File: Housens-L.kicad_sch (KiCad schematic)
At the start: 44 parts, among them J1 JTAG/SWD, J2 USB_C_2.0, Q1 DMC3071LVT, SW1 RESET, SW2 USER_BTN, U1 MCP1603, U2 BME280, U3 OPT3005, U4 STM32WB55CGUx, Y1 32MHz, Y2 32.768kHz

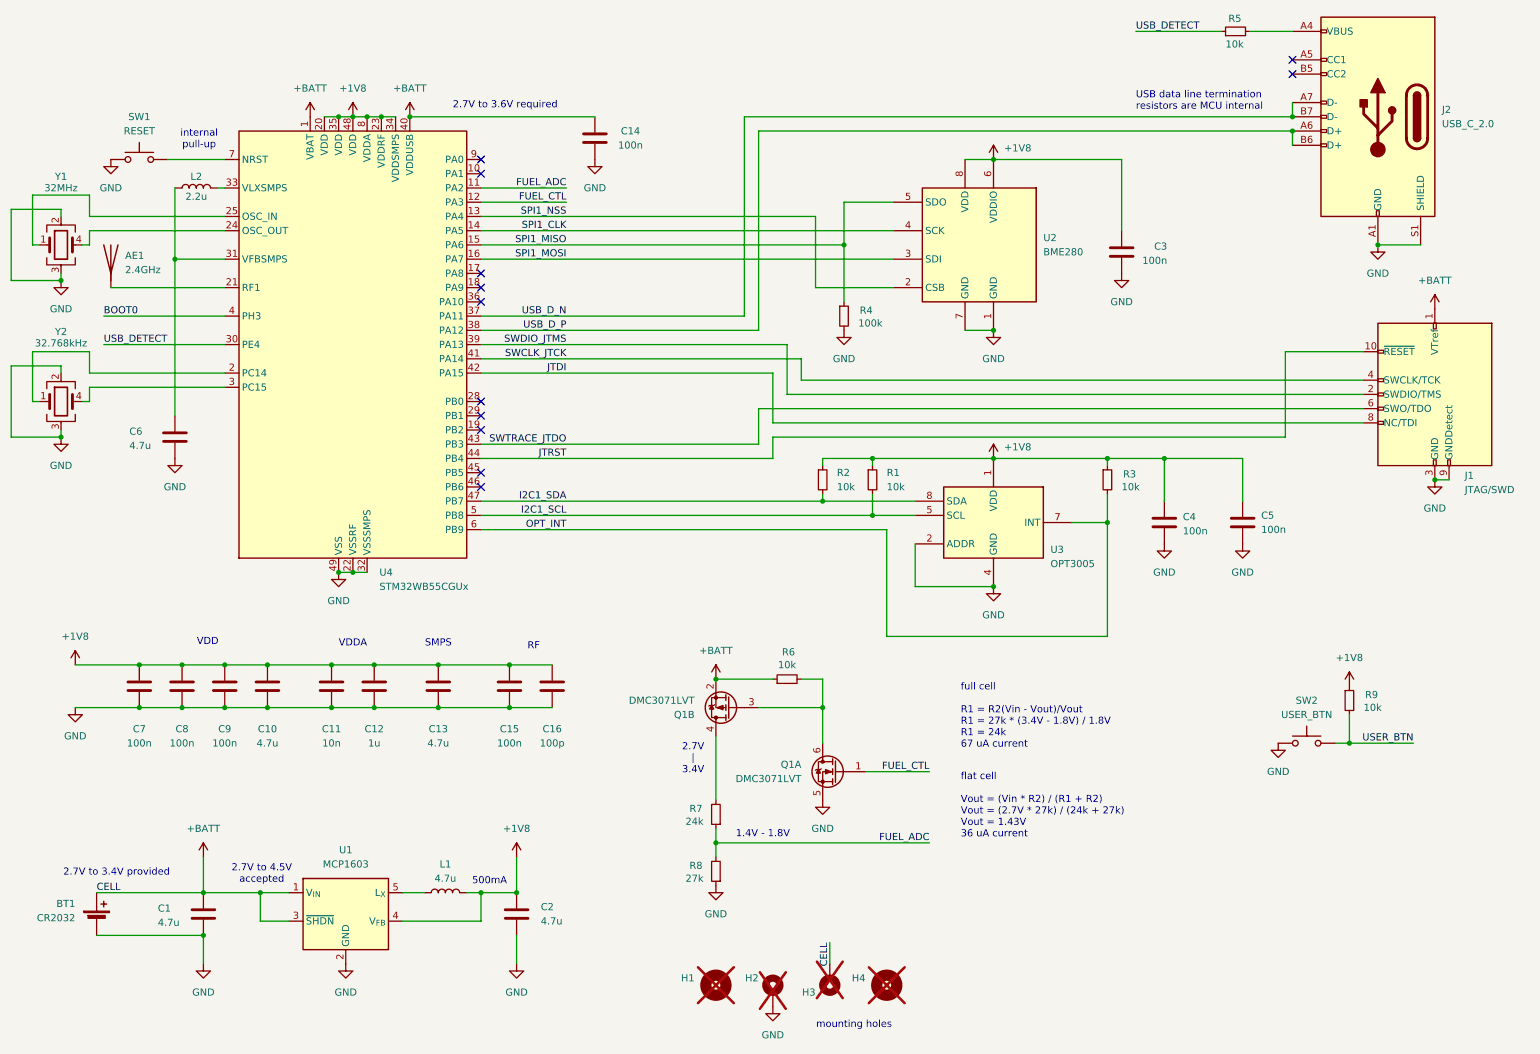
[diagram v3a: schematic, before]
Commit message: Layout 1V8 and USB
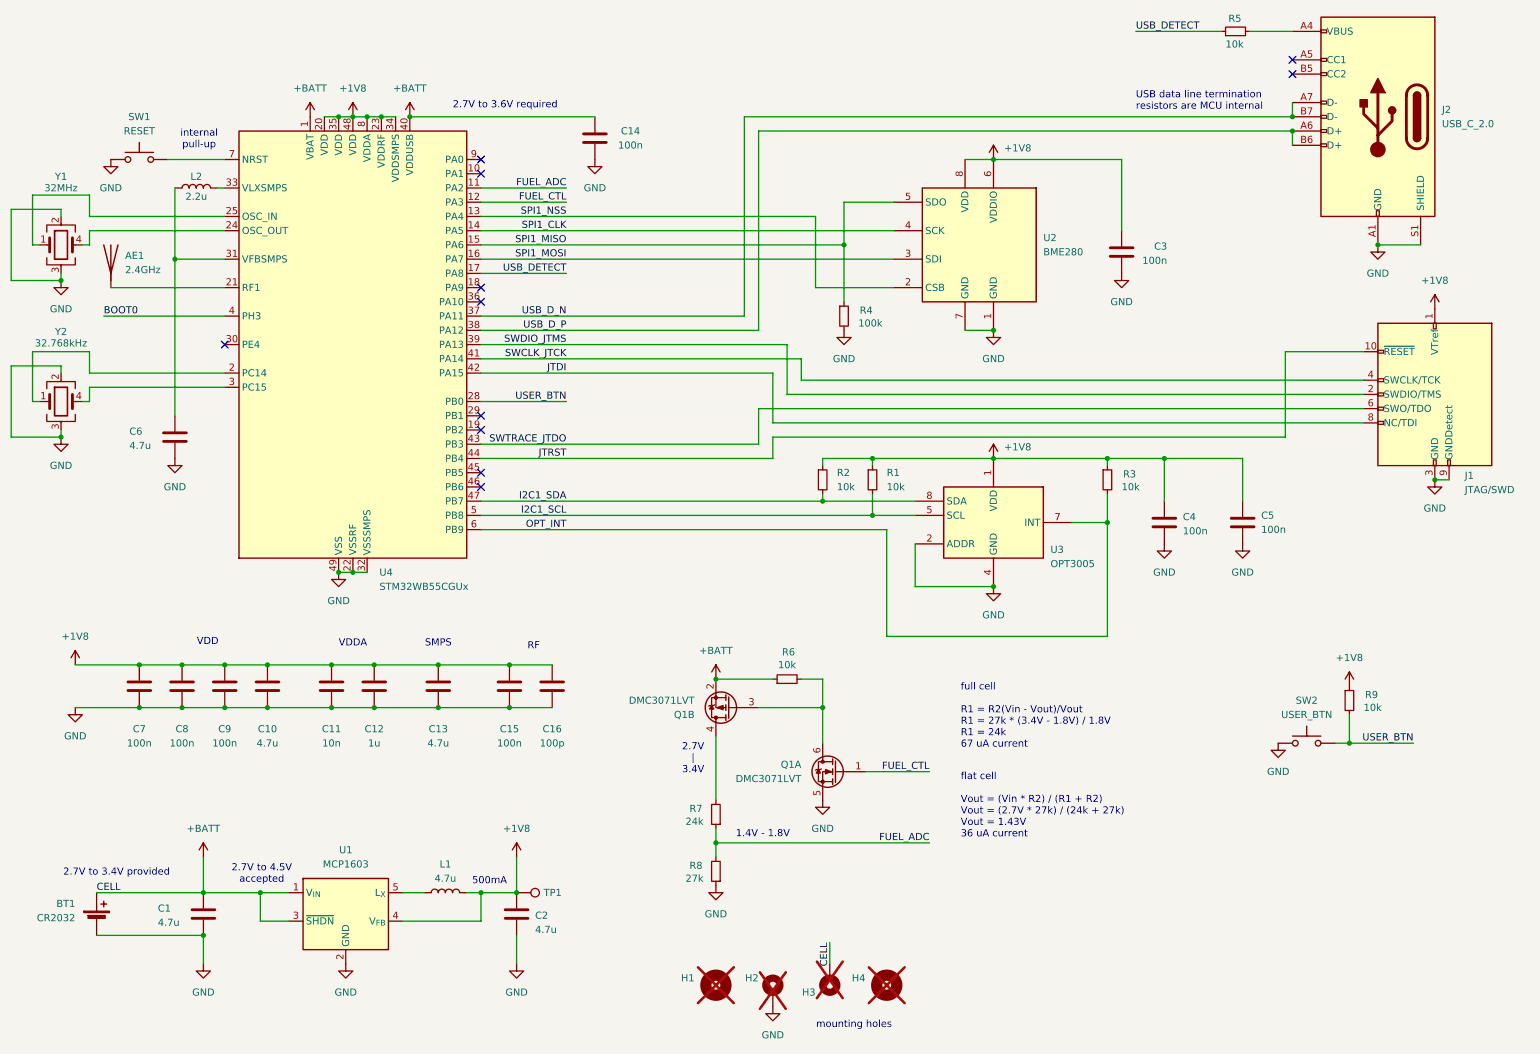
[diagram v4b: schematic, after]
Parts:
- added TP1: TestPoint, TestPoint:TestPoint_Pad_D2.0mm, symbol Connector:TestPoint
- J2: footprint Connector_USB:USB_C_Receptacle_G-Switch_GT-USB-7010ASV -> Connector_USB:USB_C_Receptacle_GCT_USB4085
- L1, L2: footprint Inductor_SMD:L_Wuerth_WE-TPC-3816 -> Imported:L_Wuerth_WE-TPC-2811
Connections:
- net +1V8: now also J1.1 (VTref), TP1.1
- net +BATT: no longer J1.1 (VTref)
- net USB_DETECT: now also U4.17 (PA8); no longer U4.30 (PE4)
- net USER_BTN: now also U4.28 (PB0)
- no-connect marks 12 -> 11
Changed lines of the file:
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@@
 	)
 	(no_connect
-		(at 99.06 82.55)
-	)
-	(no_connect
 		(at 99.06 87.63)
 	)
@@
 	)
 	(no_connect
-		(at 99.06 59.69)
-	)
-	(no_connect
 		(at 99.06 64.77)
 	)
@@
 	)
 	(no_connect
+		(at 53.34 72.39)
+	)
+	(no_connect
 		(at 99.06 62.23)
 	)
@@
 	(wire
 		(pts
-			(xy 160.02 92.71) (xy 168.91 92.71)
+			(xy 99.06 82.55) (xy 114.3 82.55)
 		)
 		(stroke
@@
 	(wire
 		(pts
-			(xy 76.2 31.75) (xy 78.74 31.75)
+			(xy 160.02 92.71) (xy 168.91 92.71)
 		)
 		(stroke
@@
 	(wire
 		(pts
-			(xy 105.41 163.83) (xy 105.41 170.18)
+			(xy 76.2 31.75) (xy 78.74 31.75)
 		)
 		(stroke
@@
 	(wire
 		(pts
-			(xy 73.66 31.75) (xy 76.2 31.75)
+			(xy 105.41 163.83) (xy 105.41 170.18)
 		)
 		(stroke
@@
 	(wire
 		(pts
-			(xy 24.13 76.2) (xy 15.24 76.2)
+			(xy 73.66 31.75) (xy 76.2 31.75)
 		)
 		(stroke
@@
 	(wire
 		(pts
-			(xy 140.97 142.24) (xy 140.97 153.67)
+			(xy 24.13 76.2) (xy 15.24 76.2)
 		)
 		(stroke
@@
 	(wire
 		(pts
-			(xy 31.75 72.39) (xy 53.34 72.39)
+			(xy 140.97 142.24) (xy 140.97 153.67)
 		)
 		(stroke
@@
 	(wire
 		(pts
+			(xy 99.06 59.69) (xy 114.3 59.69)
+		)
+		(stroke
+			(width 0)
+			(type default)
+		)
+	)
+	(wire
+		(pts
 			(xy 80.01 129.54) (xy 91.44 129.54)
 		)
@@
 		)
 	)
+	(label "USER_BTN"
+		(at 114.3 82.55 180)
+		(fields_autoplaced yes)
+		(effects
+			(font
+				(size 1.27 1.27)
+			)
+			(justify right bottom)
+		)
+	)
 	(label "FUEL_ADC"
 		(at 114.3 44.45 180)
@@
 	)
 	(label "USB_DETECT"
-		(at 31.75 72.39 0)
+		(at 114.3 59.69 180)
 		(fields_autoplaced yes)
 		(effects
@@
 				(size 1.27 1.27)
 			)
-			(justify left bottom)
+			(justify right bottom)
 		)
 	)
@@
 			)
 		)
-		(property "Footprint" "Connector_USB:USB_C_Receptacle_G-Switch_GT-USB-7010ASV"
+		(property "Footprint" "Connector_USB:USB_C_Receptacle_GCT_USB4085"
 			(at 255.27 31.75 0)
 			(effects
@@
 	)
 	(symbol
-		(lib_id "power:+BATT")
-		(at 269.24 66.04 0)
-		(unit 1)
-		(exclude_from_sim no)
-		(in_bom yes)
-		(on_board yes)
-		(dnp no)
-		(fields_autoplaced yes)
-		(property "Reference" "#PWR023"
-			(at 269.24 69.85 0)
-			(effects
-				(font
-					(size 1.27 1.27)
-				)
-				(hide yes)
-			)
-		)
-		(property "Value" "+BATT"
-			(at 269.24 60.96 0)
-			(effects
-				(font
-					(size 1.27 1.27)
-				)
-			)
-		)
-		(property "Footprint" ""
-			(at 269.24 66.04 0)
-			(effects
-				(font
-					(size 1.27 1.27)
-				)
-				(hide yes)
-			)
-		)
-		(property "Datasheet" ""
-			(at 269.24 66.04 0)
-			(effects
-				(font
-					(size 1.27 1.27)
-				)
-				(hide yes)
-			)
-		)
-		(property "Description" "Power symbol creates a global label with name \"+BATT\""
-			(at 269.24 66.04 0)
-			(effects
-				(font
-					(size 1.27 1.27)
-				)
-				(hide yes)
-			)
-		)
-		(pin "1"
-		)
-		(instances
-			(project "Housens-L"
-				(path "/36bb4837-104c-4aa4-b300-0e6d0ff24db5"
-					(reference "#PWR023")
-					(unit 1)
-				)
-			)
-		)
-	)
-	(symbol
 		(lib_id "power:GND")
 		(at 73.66 113.03 0)
@@
 			)
 		)
-		(property "Footprint" "Inductor_SMD:L_Wuerth_WE-TPC-3816"
+		(property "Footprint" "Imported:L_Wuerth_WE-TPC-2811"
 			(at 92.71 170.18 0)
 			(effects
@@
 			)
 		)
-		(property "Datasheet" "~"
+		(property "Datasheet" "https://www.we-online.com/components/products/datasheet/744028004.pdf"
 			(at 92.71 170.18 0)
 			(effects
@@
 			)
 		)
-		(property "Description" "Inductor"
+		(property "Description" "WE-TPC SMT Shielded Tiny Power Inductor, 4.7uH"
 			(at 92.71 170.18 0)
 			(effects
@@
 	)
 	(symbol
+		(lib_id "Connector:TestPoint")
+		(at 105.41 170.18 270)
+		(unit 1)
+		(exclude_from_sim no)
+		(in_bom yes)
+		(on_board yes)
+		(dnp no)
+		(property "Reference" "TP1"
+			(at 110.236 170.18 90)
+			(effects
+				(font
+					(size 1.27 1.27)
+				)
+				(justify left)
+			)
+		)
+		(property "Value" "TestPoint"
+			(at 110.49 171.4499 90)
+			(effects
+				(font
+					(size 1.27 1.27)
+				)
+				(justify left)
+				(hide yes)
+			)
+		)
+		(property "Footprint" "TestPoint:TestPoint_Pad_D2.0mm"
+			(at 105.41 175.26 0)
+			(effects
+				(font
+					(size 1.27 1.27)
+				)
+				(hide yes)
+			)
+		)
+		(property "Datasheet" "~"
+			(at 105.41 175.26 0)
+			(effects
+				(font
+					(size 1.27 1.27)
+				)
+				(hide yes)
+			)
+		)
+		(property "Description" "test point"
+			(at 105.41 170.18 0)
+			(effects
+				(font
+					(size 1.27 1.27)
+				)
+				(hide yes)
+			)
+		)
+		(pin "1"
+		)
+		(instances
+			(project ""
+				(path "/36bb4837-104c-4aa4-b300-0e6d0ff24db5"
+					(reference "TP1")
+					(unit 1)
+				)
+			)
+		)
+	)
+	(symbol
 		(lib_id "power:GND")
 		(at 269.24 96.52 0)
@@
 			)
 		)
-		(property "Footprint" "Inductor_SMD:L_Wuerth_WE-TPC-3816"
+		(property "Footprint" "Imported:L_Wuerth_WE-TPC-2811"
 			(at 48.26 44.45 0)
 			(effects
@@
 			)
 		)
-		(property "Datasheet" "~"
+		(property "Datasheet" "https://www.we-online.com/components/products/datasheet/744028002.pdf"
 			(at 48.26 44.45 0)
 			(effects
@@
 			)
 		)
-		(property "Description" "Inductor"
+		(property "Description" "WE-TPC SMT Shielded Tiny Power Inductor, 2.2uH"
 			(at 48.26 44.45 0)
 			(effects
@@
 		(dnp no)
 		(property "Reference" "C2"
-			(at 109.728 172.72 0)
+			(at 108.712 174.244 0)
 			(effects
 				(font
@@
 		)
 		(property "Value" "4.7u"
-			(at 109.728 175.26 0)
+			(at 108.712 176.784 0)
 			(effects
 				(font
@@
 					(unit 1)
 				)
+			)
+		)
+	)
+	(symbol
+		(lib_id "power:+1V8")
+		(at 269.24 66.04 0)
+		(unit 1)
+		(exclude_from_sim no)
+		(in_bom yes)
+		(on_board yes)
+		(dnp no)
+		(fields_autoplaced yes)
+		(property "Reference" "#PWR023"
+			(at 269.24 69.85 0)
+			(effects
+				(font
+					(size 1.27 1.27)
+				)
+				(hide yes)
+			)
+		)
+		(property "Value" "+1V8"
+			(at 269.24 60.96 0)
+			(effects
+				(font
+					(size 1.27 1.27)
+				)
+			)
+		)
+		(property "Footprint" ""
+			(at 269.24 66.04 0)
+			(effects
+				(font
+					(size 1.27 1.27)
+				)
+				(hide yes)
+			)
+		)
+		(property "Datasheet" ""
+			(at 269.24 66.04 0)
+			(effects
+				(font
+					(size 1.27 1.27)
+				)
+				(hide yes)
+			)
+		)
+		(property "Description" "Power symbol creates a global label with name \"+1V8\""
+			(at 269.24 66.04 0)
+			(effects
+				(font
+					(size 1.27 1.27)
+				)
+				(hide yes)
+			)
+		)
+		(pin "1"
+		)
+		(instances
+			(project "Housens-L"
+				(path "/36bb4837-104c-4aa4-b300-0e6d0ff24db5"
+					(reference "#PWR023")
+					(unit 1)
+				)

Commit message: Add 3D model for cell holder
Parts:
- BT1: footprint Battery:BatteryHolder_Keystone_3002_1x2032 -> Invented:BAT-HLD-001_3Pins
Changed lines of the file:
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@@
 			)
 		)
-		(property "Footprint" "Battery:BatteryHolder_Keystone_3002_1x2032"
+		(property "Footprint" "Invented:BAT-HLD-001_3Pins"
 			(at 30.48 173.736 90)
 			(effects
@@
 			)
 		)
-		(property "Datasheet" "~"
+		(property "Datasheet" "https://www.mouser.com/datasheet/2/418/9/LNNC_S_A0002913840_1-3237435.pdf"
 			(at 30.48 173.736 90)
 			(effects
@@
 			)
 		)
-		(property "Description" "Single-cell battery"
+		(property "Description" "Linx/TE SMT Battery Holder for CR2032/CR2025"
 			(at 30.48 175.26 0)
 			(effects

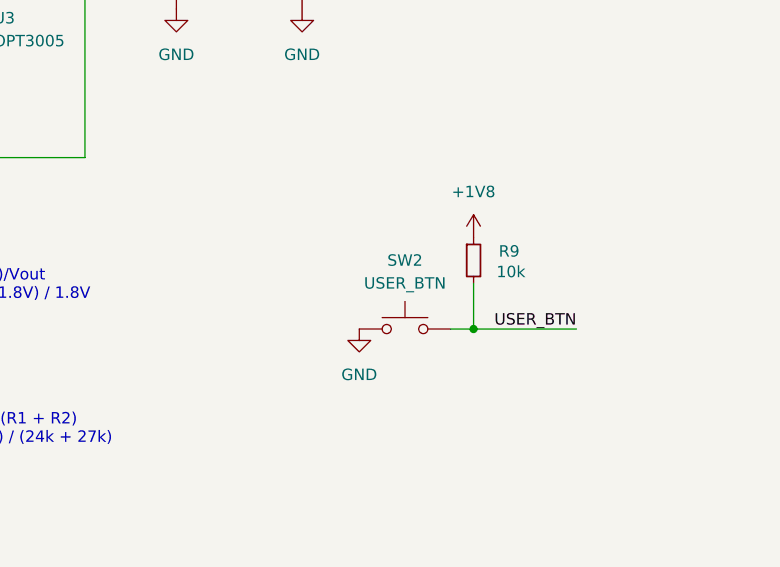
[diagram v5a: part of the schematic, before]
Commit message: Show some labels
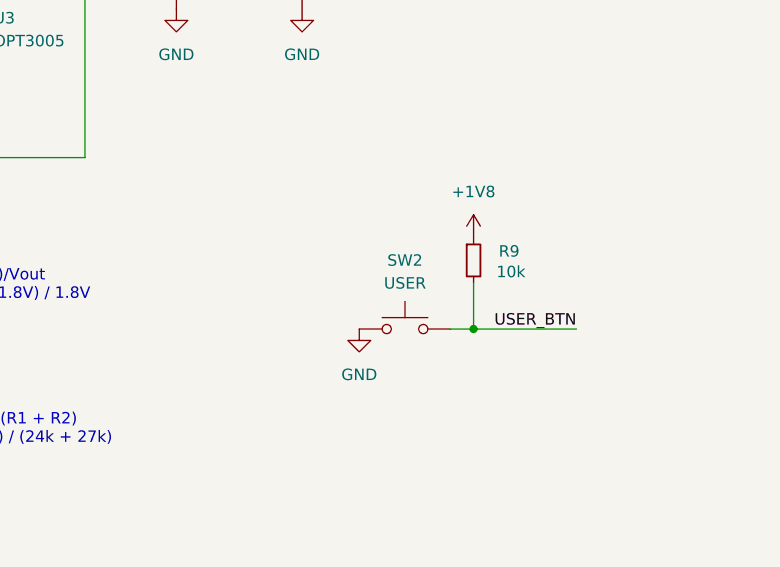
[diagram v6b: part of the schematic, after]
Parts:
- SW2: value USER_BTN -> USER
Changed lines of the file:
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@@
 			)
 		)
-		(property "Value" "USER_BTN"
+		(property "Value" "USER"
 			(at 246.38 138.43 0)
 			(effects

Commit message: Layout I2C
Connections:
- net BOOT0 is gone; now on net GND: U4.4 (PH3)
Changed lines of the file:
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@@
 	)
 	(junction
+		(at 40.64 67.31)
+		(diameter 0)
+		(color 0 0 0 0)
+	)
+	(junction
 		(at 163.83 54.61)
 		(diameter 0)
@@
 	(wire
 		(pts
-			(xy 31.75 67.31) (xy 53.34 67.31)
+			(xy 31.75 67.31) (xy 40.64 67.31)
 		)
 		(stroke
@@
 	(wire
 		(pts
+			(xy 40.64 67.31) (xy 53.34 67.31)
+		)
+		(stroke
+			(width 0)
+			(type default)
+		)
+	)
+	(wire
+		(pts
 			(xy 24.13 49.53) (xy 24.13 48.26)
 		)
@@
 					(unit 1)
 				)
+			)
+		)
+	)
+	(symbol
+		(lib_id "power:GND")
+		(at 40.64 67.31 0)
+		(unit 1)
+		(exclude_from_sim no)
+		(in_bom yes)
+		(on_board yes)
+		(dnp no)
+		(fields_autoplaced yes)
+		(property "Reference" "#PWR034"
+			(at 40.64 73.66 0)
+			(effects
+				(font
+					(size 1.27 1.27)
+				)
+				(hide yes)
+			)
+		)
+		(property "Value" "GND"
+			(at 40.64 72.39 0)
+			(effects
+				(font
+					(size 1.27 1.27)
+				)
+			)
+		)
+		(property "Footprint" ""
+			(at 40.64 67.31 0)
+			(effects
+				(font
+					(size 1.27 1.27)
+				)
+				(hide yes)
+			)
+		)
+		(property "Datasheet" ""
+			(at 40.64 67.31 0)
+			(effects
+				(font
+					(size 1.27 1.27)
+				)
+				(hide yes)
+			)
+		)
+		(property "Description" "Power symbol creates a global label with name \"GND\" , ground"
+			(at 40.64 67.31 0)
+			(effects
+				(font
+					(size 1.27 1.27)
+				)
+				(hide yes)
+			)
+		)
+		(pin "1"
+		)
+		(instances
+			(project "Housens-L"
+				(path "/36bb4837-104c-4aa4-b300-0e6d0ff24db5"
+					(reference "#PWR034")
+					(unit 1)
+				)

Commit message: Impedance-match USB lines
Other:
- title: (none) -> Housens HTP-L
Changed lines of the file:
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@@
 	(generator_version "8.0")
 	(paper "A4")
+	(title_block
+		(title "Housens HTP-L")
+		(date "2025-01-26")
+		(rev "001")
+	)
 	(junction
 		(at 104.14 129.54)
